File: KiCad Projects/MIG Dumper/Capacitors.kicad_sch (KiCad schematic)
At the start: 33 parts

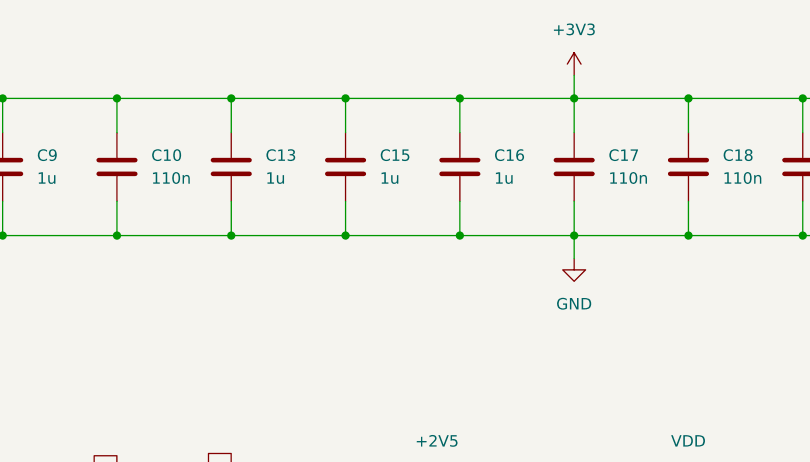
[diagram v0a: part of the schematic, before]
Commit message: Updated Flashcart PCB, uploaded Flashcart BOM
Revised the Flashcart PCB to the newer revision of the MIG v2, as well as added DigiKey and Mouser BOMs for the Flashcart. One capacitor measurement on the Dumper PCB was corrected as well.
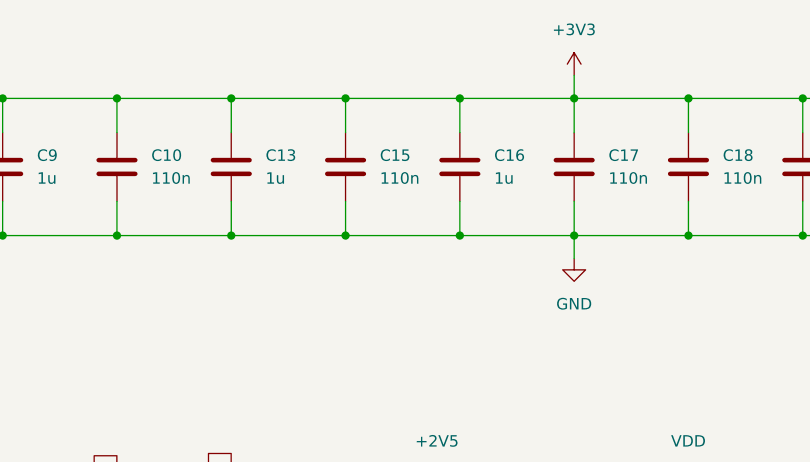
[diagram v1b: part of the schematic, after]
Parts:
- C15: value 1u -> 110n
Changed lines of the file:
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@@
 			)
 		)
-		(property "Value" "1u"
+		(property "Value" "110n"
 			(at 127 53.3399 0)
 			(effects
